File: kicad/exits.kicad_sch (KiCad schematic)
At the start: 66 parts, among them J1 PJ301M12, J12 Euro power header, J13 SJ-63083A, J14 PJ301M12, J2 PJ301M12, J3 PJ301M12, J4 PJ301M12, J5 Attenuator Jumper 1, J6 Attenuator Jumper 1, U1 TL074, U2 RC4580

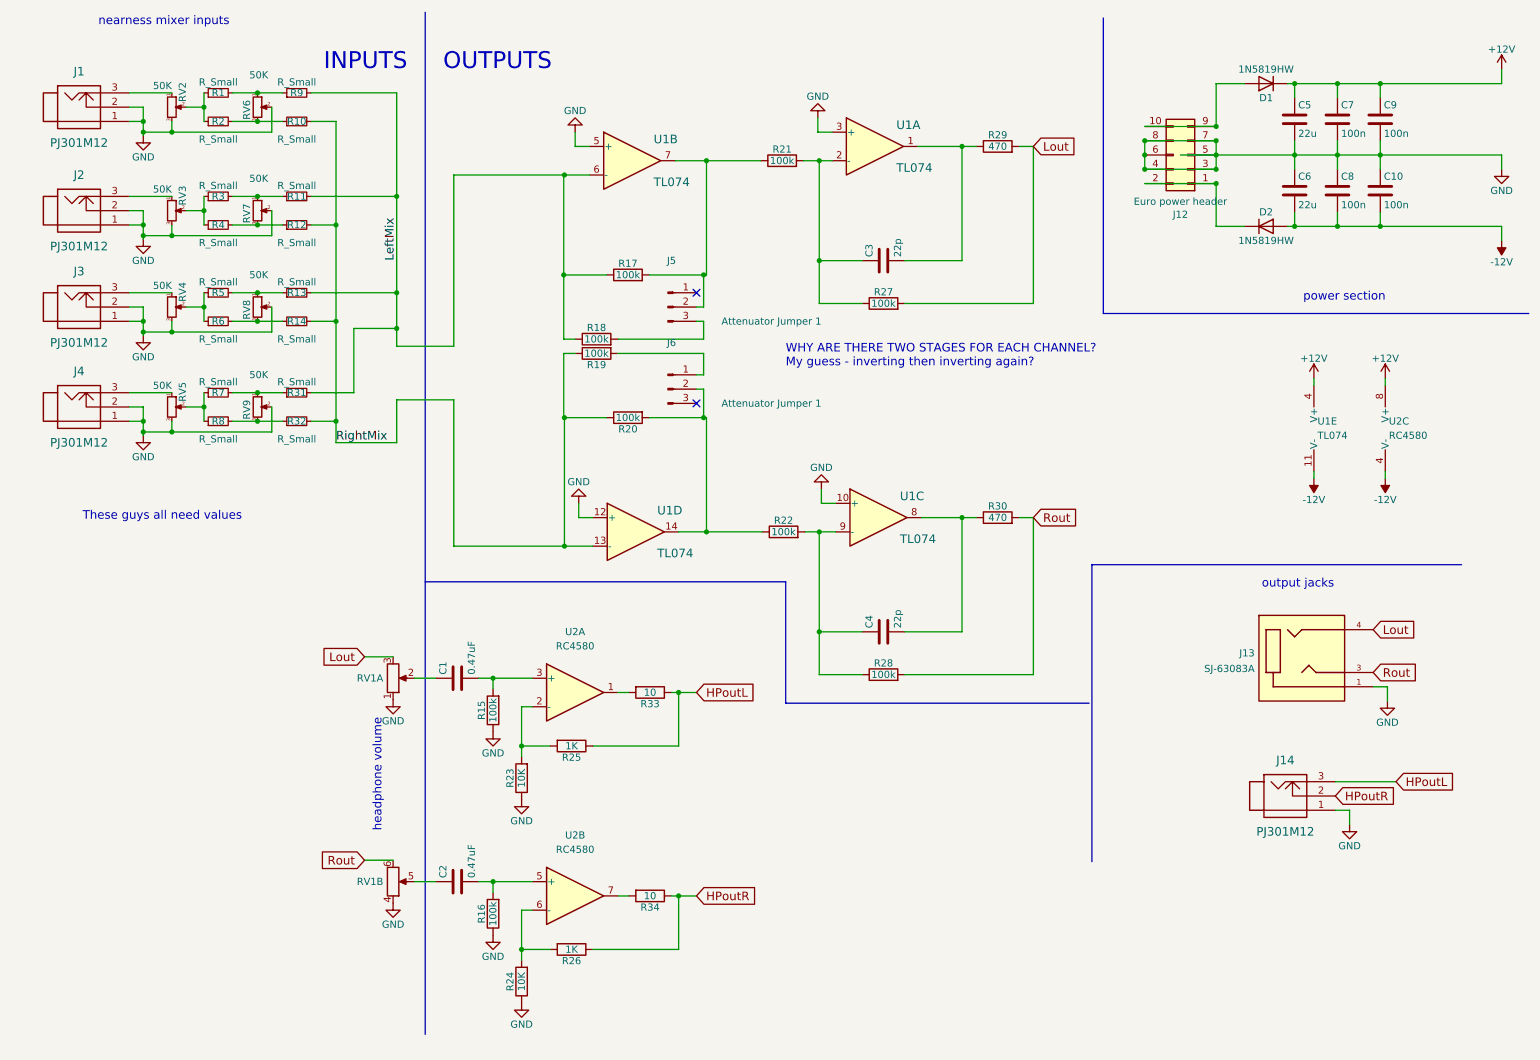
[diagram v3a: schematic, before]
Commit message: Switched to non-inverting amp config, tweaked values
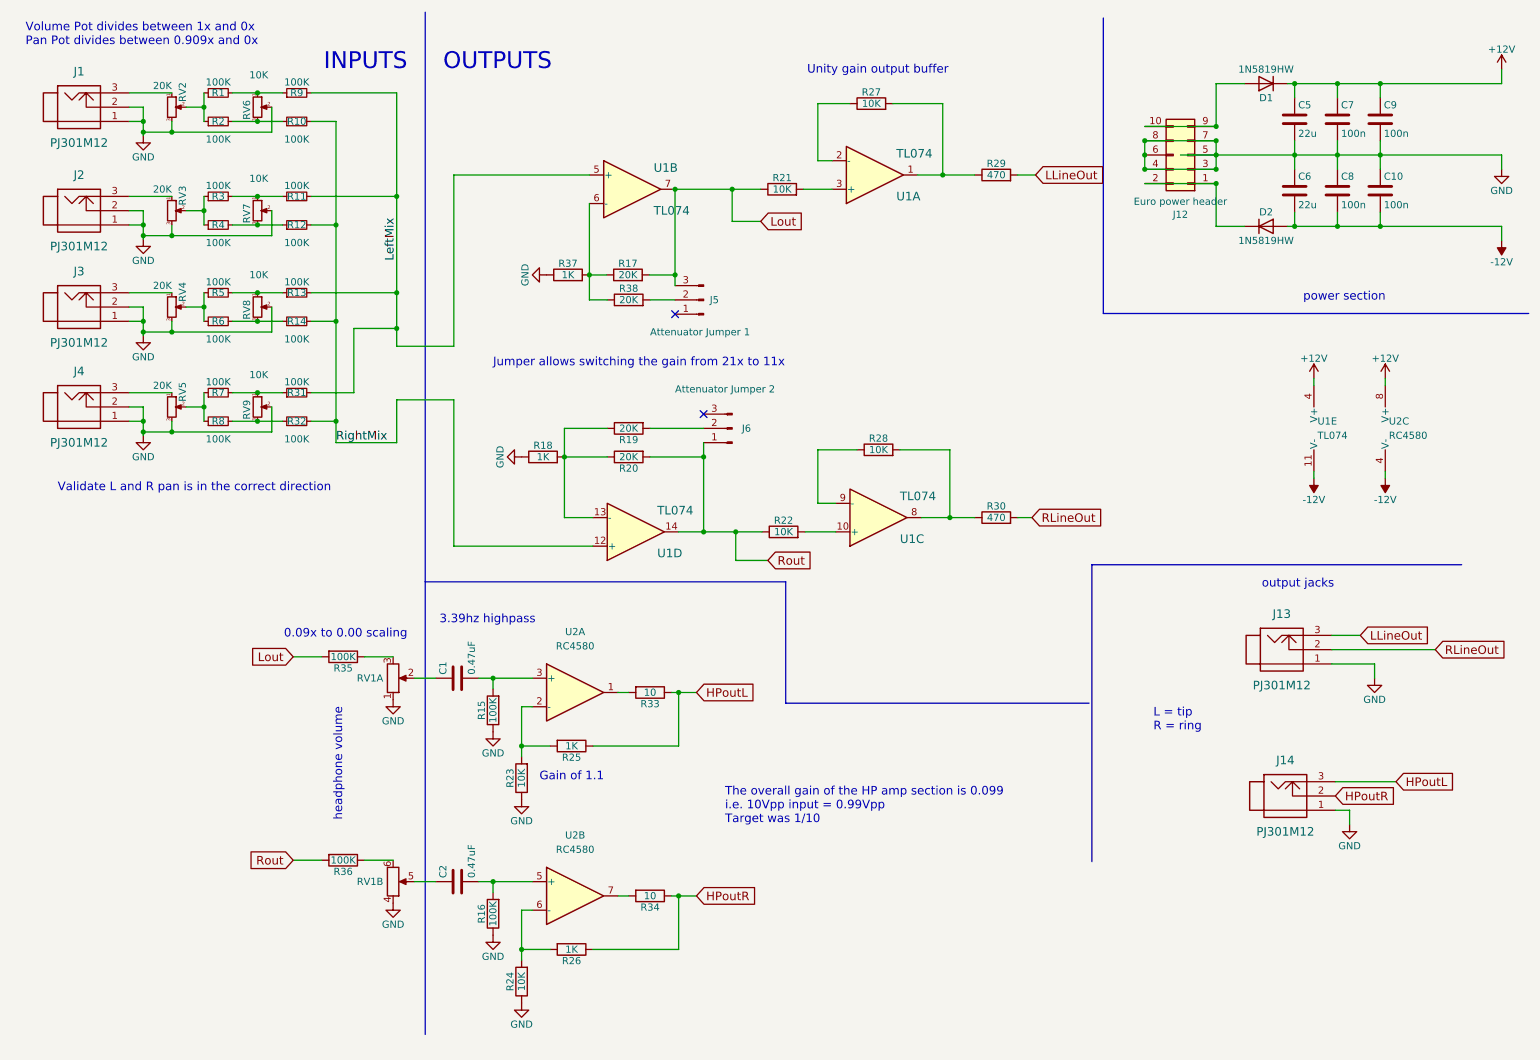
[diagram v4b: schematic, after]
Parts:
- removed C3, C4: 22p, nearness:0603, symbol Device:C
- removed J13: SJ-63083A, Connector:CUI_SJ-63083A, symbol SJ-63083A:SJ-63083A
- added J13: PJ301M12, nearness:PJ301M12, symbol pj301m12:PJ301M12
- added R35, R36: 100K, Resistor_SMD:R_0805_2012Metric, symbol Device:R
- added R37: 1K, Resistor_SMD:R_0603_1608Metric, symbol Device:R
- added R38: 20K, Resistor_SMD:R_0603_1608Metric, symbol Device:R
- C10, C7, C8, C9: footprint nearness:0603 -> Capacitor_SMD:C_0603_1608Metric
- C5, C6: footprint nearness:0805 -> Capacitor_SMD:C_0805_2012Metric
- J6: value Attenuator Jumper 1 -> Attenuator Jumper 2
- R1, R10, R11, R12, R13, R14, R2, R3, R31, R32, R4, R5, R6, R7, R8, R9: value R_Small -> 100K; footprint nearness:0603 -> Resistor_SMD:R_0603_1608Metric
- R15, R16: value 100k -> 100K; footprint Resistor_SMD:R_1206_3216Metric -> Resistor_SMD:R_0805_2012Metric
- R17, R19, R20: value 100k -> 20K; footprint nearness:0603 -> Resistor_SMD:R_0603_1608Metric
- R18: value 100k -> 1K; footprint nearness:0603 -> Resistor_SMD:R_0603_1608Metric
- R21, R22, R27, R28: value 100k -> 10K; footprint nearness:0603 -> Resistor_SMD:R_0603_1608Metric
- R23, R24, R25, R26: footprint Resistor_SMD:R_1206_3216Metric -> Resistor_SMD:R_0805_2012Metric
- R29, R30: footprint nearness:0603 -> Resistor_SMD:R_0603_1608Metric
- RV1: value 50KA -> B10K
- RV2, RV3, RV4, RV5: value 50K -> 20K
- RV6, RV7, RV8, RV9: value 50K -> 10K
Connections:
- net GND: now also R18.1, J13.1, R37.1; no longer U1.10 (+), U1.12 (+), U1.3 (+), U1.5 (+)
- net LeftMix: now also U1.5 (+); no longer R17.1, R18.1
- net Lout: now also J5.3 (Pin_3), R17.2, R21.1, U1.7, R35.2; no longer R27.2, R29.2, RV1.3
- net RightMix: now also U1.12 (+); no longer R19.1, R20.1, U1.13 (-)
- net Rout: now also J6.1 (Pin_1), R20.2, R22.1, U1.14, R36.2; no longer R28.2, R30.2, RV1.6
- net at R29.1, U1.1: now also R27.2
- net at R30.1, U1.8: now also R28.2
- net at R27.1, U1.2 (-): no longer R21.2
- net at R28.1, U1.9 (-): no longer R22.2
- net at U1.6 (-): now also R17.1, R37.2, R38.1
- net at R18.2: now also R19.1, R20.1, U1.13 (-); no longer J5.3 (Pin_3)
- net at R19.2: now also J6.2 (Pin_2); no longer J6.1 (Pin_1)
- new net: R21.2, U1.3 (+)
- new net: R22.2, U1.10 (+)
- new net: R36.1, RV1.6
- new net: R35.1, RV1.3
- new net: J5.2 (Pin_2), R38.2
- new net LLineOut: J13.3, R29.2
- new net RLineOut: J13.2, R30.2
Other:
- note added: "0.09x to 0.00 scaling"
- note added: "3.39hz highpass"
- note added: "Gain of 1.1"
- note added: "Jumper allows switching the gain from 21x to 11x"
- note added: "L = tip R = ring"
- note added: "The overall gain of the HP amp section is 0.099 i.e. 10Vpp input = 0.99Vpp Target was 1/10"
- note added: "Unity gain output buffer"
- note added: "Validate L and R pan is in the correct direction"
- note added: "Volume Pot divides between 1x and 0x Pan Pot divides between 0.909x and 0x"
- note removed: "These guys all need values"
- note removed: "WHY ARE THERE TWO STAGES FOR EACH CHANNEL? My guess - inverting then inverting again?"
- note removed: "nearness mixer inputs"
- moved on the sheet: J5, J6, R18, R19, R20, R21, R27, R28, R29, U1A, U1B

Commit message: Switched to current mixing, updated pcb
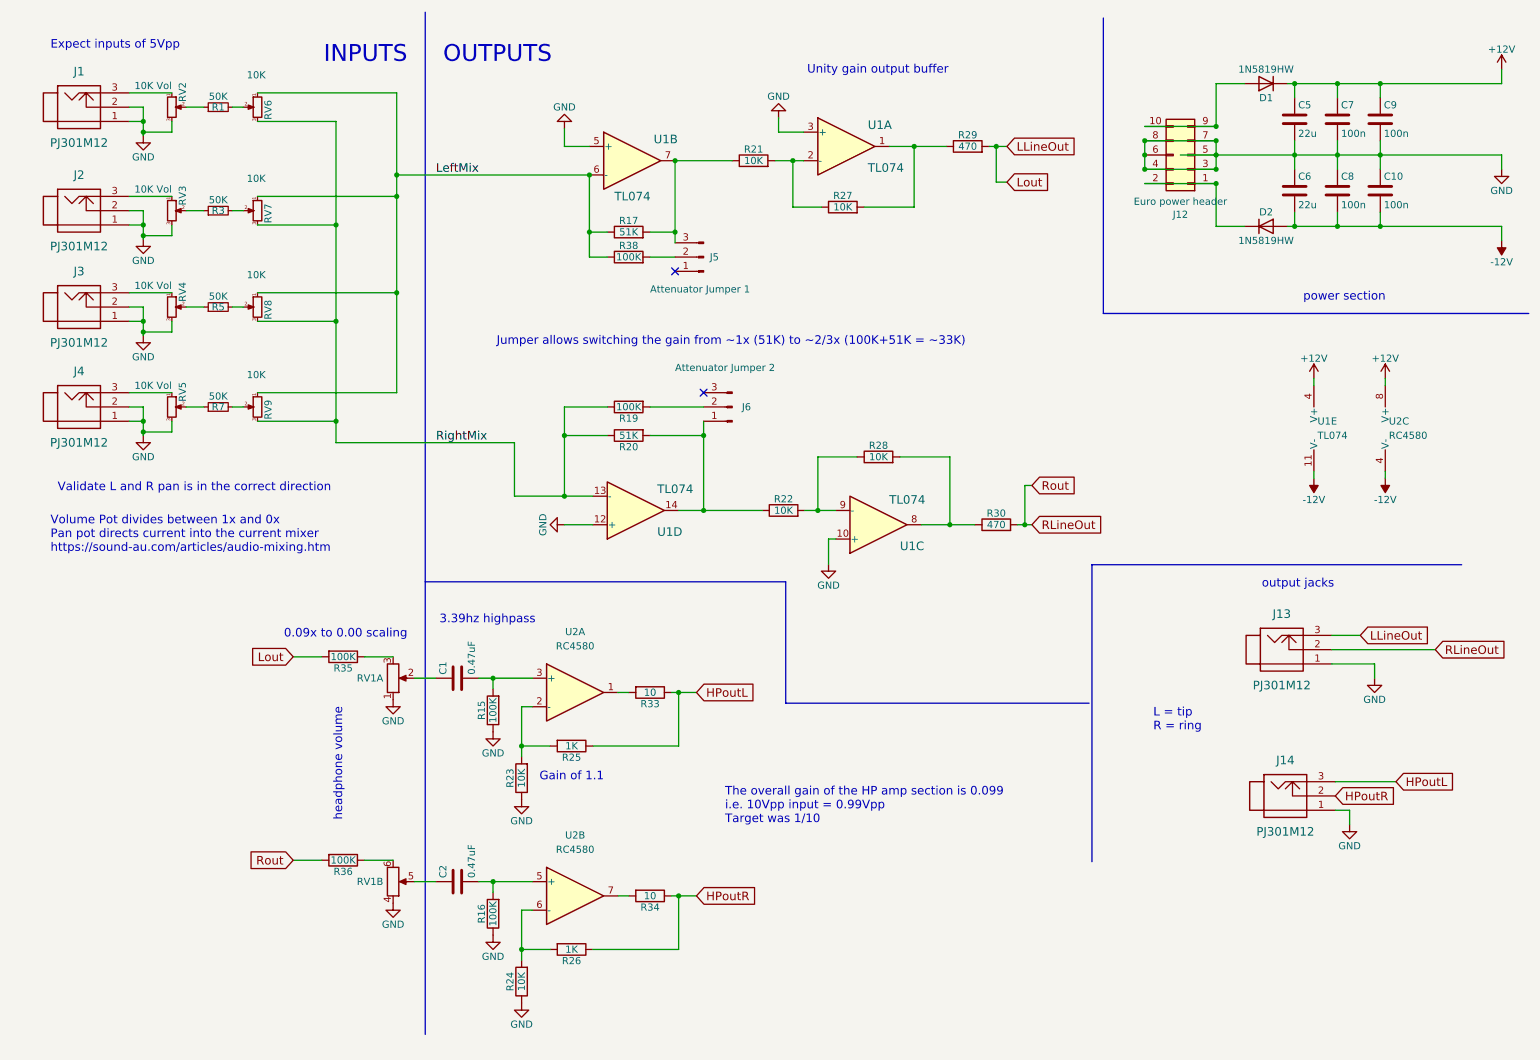
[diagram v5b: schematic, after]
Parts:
- removed R10, R11, R12, R13, R14, R2, R31, R32, R4, R6, R8, R9: 100K, Resistor_SMD:R_0603_1608Metric, symbol Device:R_Small
- removed R18, R37: 1K, Resistor_SMD:R_0603_1608Metric, symbol Device:R
- R1, R3, R5, R7: value 100K -> 50K
- R17, R20: value 20K -> 51K
- R19, R38: value 20K -> 100K
- RV2, RV3, RV4, RV5: value 20K -> 10K Vol
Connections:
- net GND: now also U1.10 (+), U1.12 (+), U1.3 (+), U1.5 (+); no longer RV6.2, RV7.2, RV8.2, RV9.2
- net LLineOut: now also R35.2
- net LeftMix: now also R17.1, R38.1, RV6.1, RV7.1, RV8.1, RV9.1, U1.6 (-); no longer U1.5 (+)
- net RLineOut: now also R36.2
- net RightMix: now also R19.1, R20.1, RV6.3, RV7.3, RV8.3, RV9.3, U1.13 (-); no longer U1.12 (+)
- net at R21.2: now also R27.1, U1.2 (-); no longer U1.3 (+)
- net at R22.2: now also R28.1, U1.9 (-); no longer U1.10 (+)
- net at R3.2: now also RV7.2; no longer RV7.1
- net at R1.2: now also RV6.2; no longer RV6.1
- net at R7.2: now also RV9.2; no longer RV9.1
- net at R5.2: now also RV8.2; no longer RV8.1
- net Lout: no longer names the net of J5.3 (Pin_3), R17.2, R21.1, U1.7
- net Lout: no longer R35.2
- net Rout: no longer names the net of J6.1 (Pin_1), R20.2, R22.1, U1.14
- net Rout: no longer R36.2
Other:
- note added: "Expect inputs of 5Vpp"
- note added: "Jumper allows switching the gain from ~1x (51K) to ~2/3x (100K+51K = ~33K)"
- note added: "Volume Pot divides between 1x and 0x Pan pot directs current into the current mixer https://sound-au.com/articles/audio-mixing.htm"
- note removed: "Jumper allows switching the gain from 21x to 11x"
- note removed: "Volume Pot divides between 1x and 0x Pan Pot divides between 0.909x and 0x"
- moved on the sheet: J5, J6, R1, R17, R19, R20, R21, R22, R27, R28, R29, R3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

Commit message: added my readme
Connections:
- net at R17.2, R21.1, U1.7: now also J5.1 (Pin_1); no longer J5.3 (Pin_3)
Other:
- moved on the sheet: J5
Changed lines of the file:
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@@
     (pin "1")
   )
-  (symbol (lib_id "Connector:Conn_01x03_Male") (at 135.89 56.515 180) (unit 1)
+  (symbol (lib_id "Connector:Conn_01x03_Male") (at 135.89 56.515 0) (mirror y) (unit 1)
     (in_bom yes) (on_board yes)
     (property "Reference" "J5" (id 0) (at 137.795 56.515 0))
-    (property "Value" "Attenuator Jumper 1" (id 1) (at 135.255 62.23 0))
+    (property "Value" "Attenuator Jumper 1" (id 1) (at 135.89 61.595 0))
     (property "Footprint" "Connector_PinHeader_2.54mm:PinHeader_1x03_P2.54mm_Vertical" (id 2) (at 135.89 56.515 0)
       (effects (font (size 1.27 1.27)) hide)
